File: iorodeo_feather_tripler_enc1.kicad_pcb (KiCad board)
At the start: 2 copper layers, 105.7 x 69.6 mm, 14 parts, among them J1 Barrel_Jack_Switch, J2 Conn_01x04, J3 Conn_01x04, J4 Conn_01x04, J5 Conn_01x04, J6 Conn_01x04, M1 MountingHole_4.3mm_M4, M2 MountingHole_4.3mm_M4, M3 MountingHole_4.3mm_M4, M4 MountingHole_4.3mm_M4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

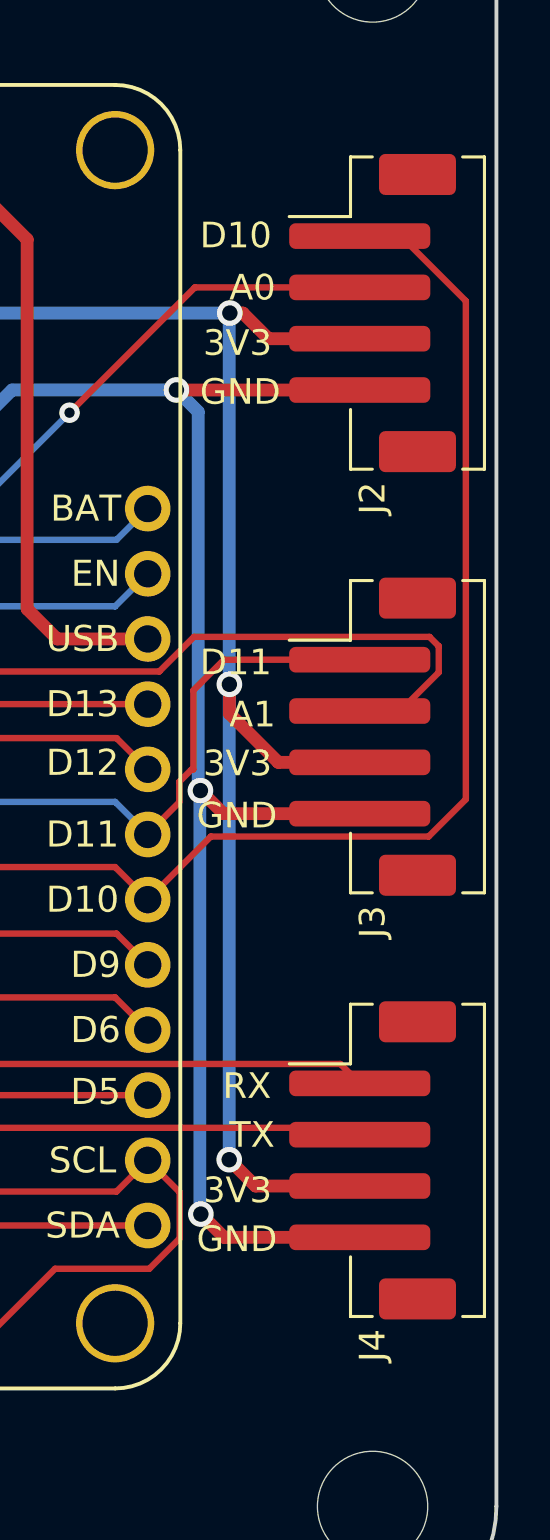
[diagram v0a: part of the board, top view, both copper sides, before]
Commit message: Fixed issues with JST PH header orientation.
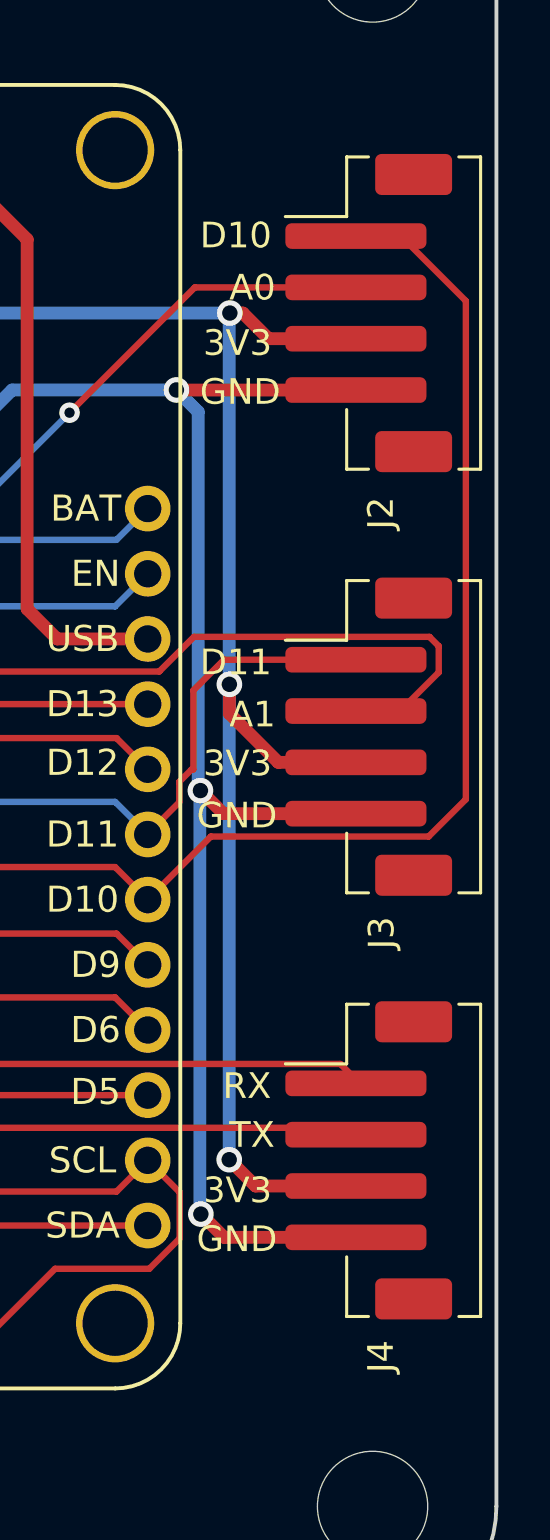
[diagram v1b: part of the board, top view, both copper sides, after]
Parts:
- J2, J3, J4: footprint Connector_JST:JST_PH_B4B-PH-SM4-TB_1x04-1MP_P2.00mm_Vertical -> JST_PH_4Pin_Vertical:JST_PH_B4B-PH-SM4-TB_1x04-1MP_P2.00mm_Vertical
- moved J2 0.40 mm to (147.2, 64.3), turned to 90 degrees
- moved J3 0.40 mm to (147.2, 80.8), turned to 90 degrees
- moved J4 0.40 mm to (147.2, 97.3), turned to 90 degrees

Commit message: Worked on revision 2.
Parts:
- moved J2 3.21 mm to (144.0, 64.3), turned to -90 degrees
- moved J3 3.21 mm to (144.0, 80.8), turned to -90 degrees
- moved J4 3.21 mm to (144.0, 97.3), turned to -90 degrees
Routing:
- net GND: track 232.6 -> 157.5 mm, vias 3 -> 0
- net /3V3: track 216.9 -> 142.4 mm, vias 4 -> 1
- net /D10: track 89.0 -> 50.4 mm
- net /A0: track 83.4 -> 51.1 mm, vias 1 -> 0
- net /RX: track 79.7 -> 50.3 mm
- net /TX: track 79.6 -> 51.0 mm
- net /A1: track 89.0 -> 72.6 mm
- net /D11: track 63.7 -> 50.4 mm

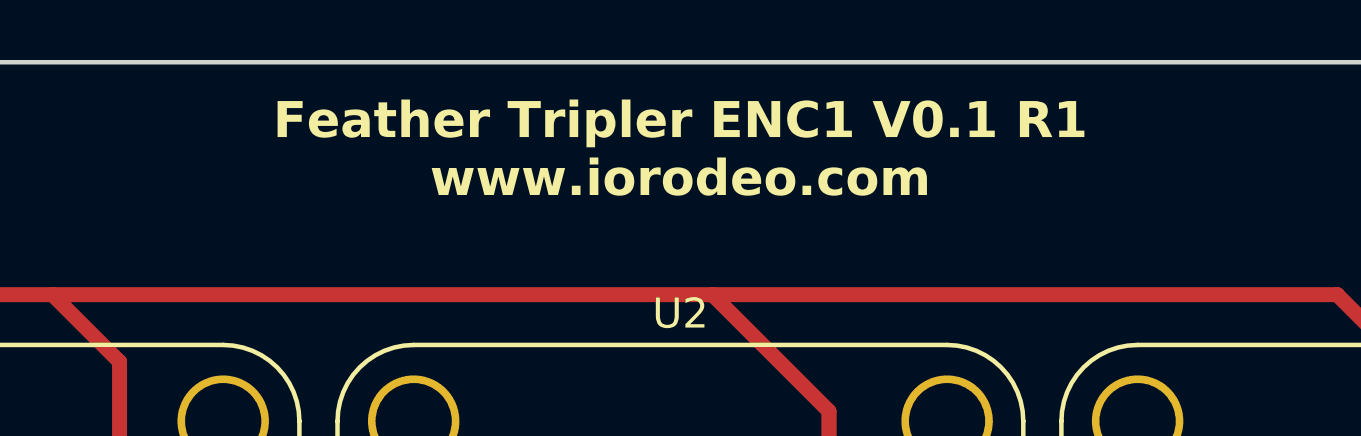
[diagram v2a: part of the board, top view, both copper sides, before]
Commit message: More work on revision 2. Added jumper pads to grove headers.
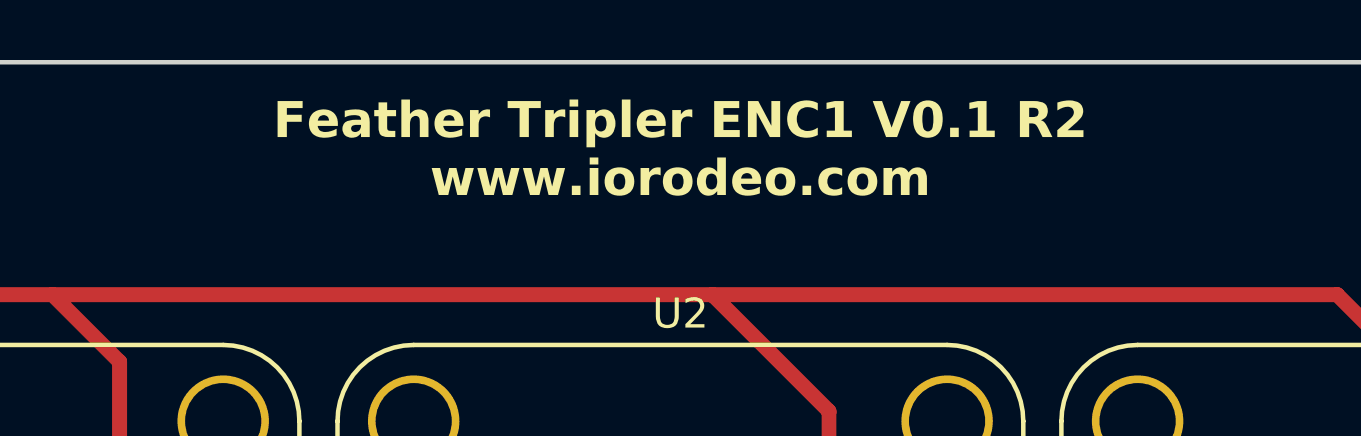
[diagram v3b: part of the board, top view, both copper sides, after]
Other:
- board text added: "Feather Tripler ENC1 V0.1 R2 www.iorodeo.com"
- board text removed: "Feather Tripler ENC1 V0.1 R1 www.iorodeo.com"
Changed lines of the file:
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@@
     (effects (font (size 1 1) (thickness 0.15)) (justify left bottom))
   )
-  (gr_text "Feather Tripler ENC1 V0.1 R1\nwww.iorodeo.com" (at 103.759 50.546) (layer "F.SilkS")
+  (gr_text "Feather Tripler ENC1 V0.1 R2\nwww.iorodeo.com" (at 103.759 50.546) (layer "F.SilkS")
     (effects (font (size 1.2 1.2) (thickness 0.25) bold) (justify bottom))
   )

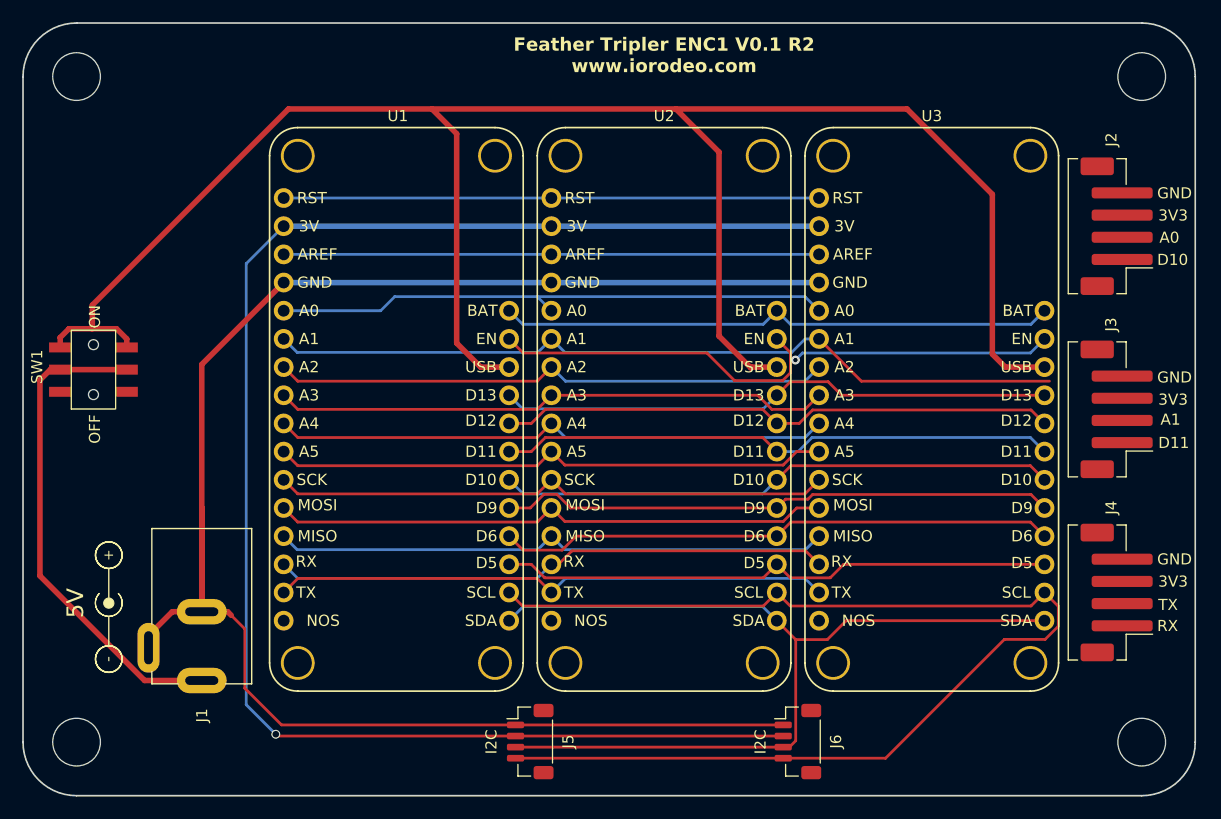
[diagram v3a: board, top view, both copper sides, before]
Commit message: Finished rerouting board.  Remade production files. Need to be checked.
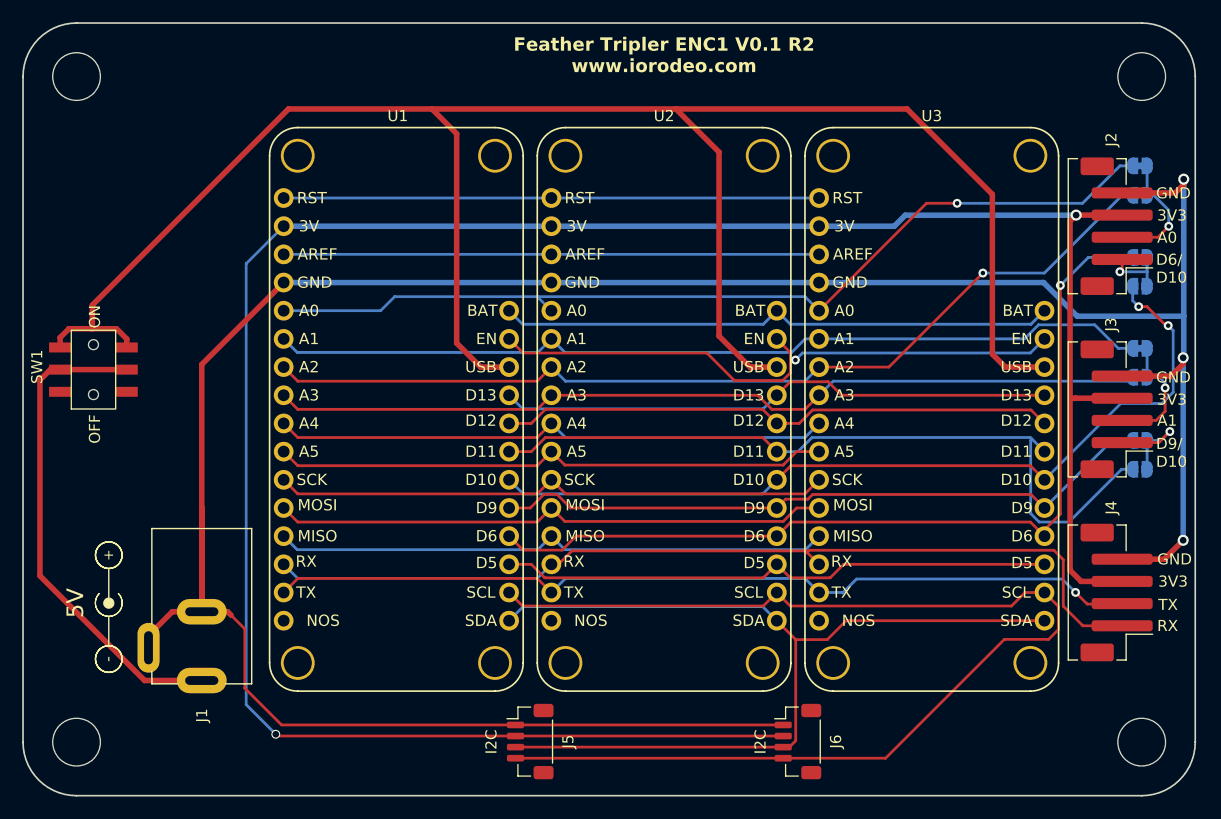
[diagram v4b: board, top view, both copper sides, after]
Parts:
- added JP1: SolderJumper_2_Bridged, Jumper:SolderJumper-2_P1.3mm_Bridged_RoundedPad1.0x1.5mm, B.Cu at (146.7, 67.1)
- added JP2: SolderJumper_2_Open, Jumper:SolderJumper-2_P1.3mm_Open_RoundedPad1.0x1.5mm, B.Cu at (146.7, 69.7)
- added JP3: SolderJumper_2_Bridged, Jumper:SolderJumper-2_P1.3mm_Bridged_RoundedPad1.0x1.5mm, B.Cu at (146.7, 58.9)
- added JP4: SolderJumper_2_Open, Jumper:SolderJumper-2_P1.3mm_Open_RoundedPad1.0x1.5mm, B.Cu at (146.7, 61.5)
- added JP5: SolderJumper_2_Bridged, Jumper:SolderJumper-2_P1.3mm_Bridged_RoundedPad1.0x1.5mm, B.Cu at (146.7, 83.6)
- added JP6: SolderJumper_2_Open, Jumper:SolderJumper-2_P1.3mm_Open_RoundedPad1.0x1.5mm, B.Cu at (146.7, 86.2)
- added JP7: SolderJumper_2_Bridged, Jumper:SolderJumper-2_P1.3mm_Bridged_RoundedPad1.0x1.5mm, B.Cu at (146.7, 75.3)
- added JP8: SolderJumper_2_Open, Jumper:SolderJumper-2_P1.3mm_Open_RoundedPad1.0x1.5mm, B.Cu at (146.7, 77.9)
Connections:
- J2 pad 1: /D10 -> Net-(J2-Pin_1)
- J2 pad 2: /A0 -> Net-(J2-Pin_2)
- J3 pad 1: /D11 -> Net-(J3-Pin_1)
- J3 pad 2: /A1 -> Net-(J3-Pin_2)
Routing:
- net GND: track 157.5 -> 243.2 mm, vias 0 -> 3
- net /3V3: track 142.4 -> 212.2 mm, vias 1 -> 2
- net /A2: track 50.4 -> 85.1 mm, vias 0 -> 1
- net /RX: track 50.3 -> 84.1 mm
- net /A0: track 51.1 -> 84.8 mm, vias 0 -> 1
- net /D6: track 50.4 -> 80.9 mm, vias 0 -> 1
- net /A3: track 50.4 -> 79.3 mm
- net /TX: track 51.0 -> 79.2 mm, vias 0 -> 1
- net /D10: track 50.4 -> 76.9 mm, vias 0 -> 2
- net /D11: track 50.4 -> 68.6 mm
- net Net-(J2-Pin_2): track 0.00 -> 11.2 mm, vias 0 -> 1
- net Net-(J3-Pin_2): track 0.00 -> 11.2 mm, vias 0 -> 1
- net /D9: track 50.3 -> 60.8 mm
- net Net-(J3-Pin_1): track 0.00 -> 9.69 mm, vias 0 -> 1
- net /A1: track 72.6 -> 80.0 mm
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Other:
- board text added: "A2"
- board text added: "A3"
- board text added: "D6"
- board text added: "D6/ D10"
- board text added: "D9/ D10"
- board text added: "J2 Pin1 Select"
- board text added: "J2 Pin2 Select"
- board text added: "J3 Pin1 Select"
- board text added: "J3 Pin2 Select"
- board text removed: "D11"

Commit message: Fixed issues in silkscreen. Remade gerbers.
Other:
- board text added: "D11"
- board text added: "D9"
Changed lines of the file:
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@@
     (effects (font (size 1 1) (thickness 0.2) bold) (justify left bottom mirror))
   )
-  (gr_text "D10" (at 151.2 86.8) (layer "B.SilkS")
+  (gr_text "D11" (at 151.2 86.8) (layer "B.SilkS")
     (effects (font (size 1 1) (thickness 0.15)) (justify left bottom mirror))
   )
-  (gr_text "D6" (at 150.4 84.2) (layer "B.SilkS")
+  (gr_text "D9" (at 150.4 84.2) (layer "B.SilkS")
     (effects (font (size 1 1) (thickness 0.15)) (justify left bottom mirror))
   )

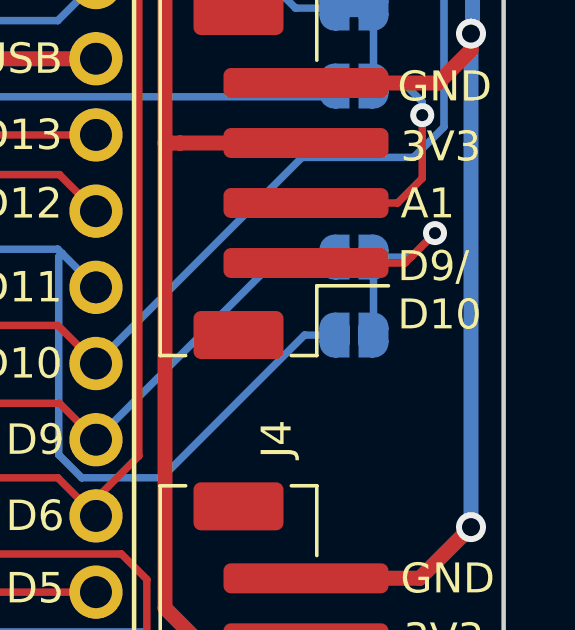
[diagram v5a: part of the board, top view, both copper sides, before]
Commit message: Fixed another issue in silkscreen and remade gerbers.
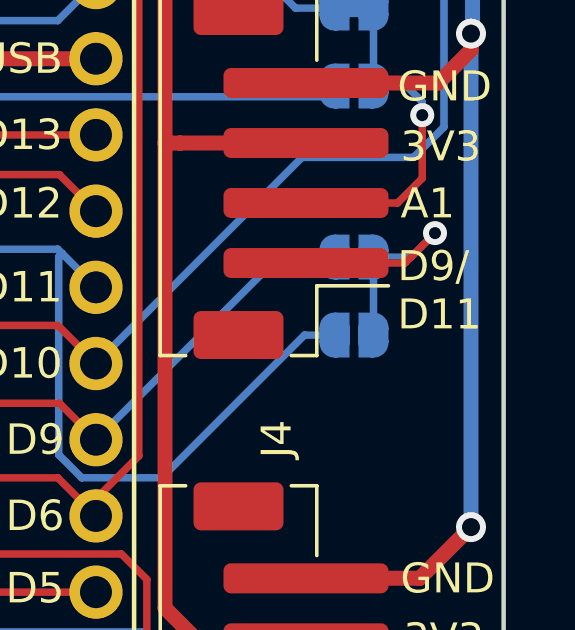
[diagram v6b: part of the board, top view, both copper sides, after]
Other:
- board text added: "D9/ D11"
- board text removed: "D9/ D10"
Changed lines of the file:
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@@
     (effects (font (size 1.5 1.5) (thickness 0.2)) (justify left bottom))
   )
-  (gr_text "D9/\nD10" (at 148.1 86.1) (layer "F.SilkS")
+  (gr_text "D9/\nD11" (at 148.1 86.1) (layer "F.SilkS")
     (effects (font (size 1 1) (thickness 0.15)) (justify left bottom))
   )
